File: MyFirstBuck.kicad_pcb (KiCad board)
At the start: 2 copper layers, 130.3 x 127 mm, 43 parts, among them J1 Conn_01x01_Pin, J2 Conn_01x01_Pin, J3 Conn_01x01_Pin, J4 Conn_01x01_Pin, J5 Conn_01x01_Pin, Q1 IRF540N, U1 LM358, U2 LAUNCHXL-F28379D, U3 UCC5304DWVR, U4 TMV 0512SHI

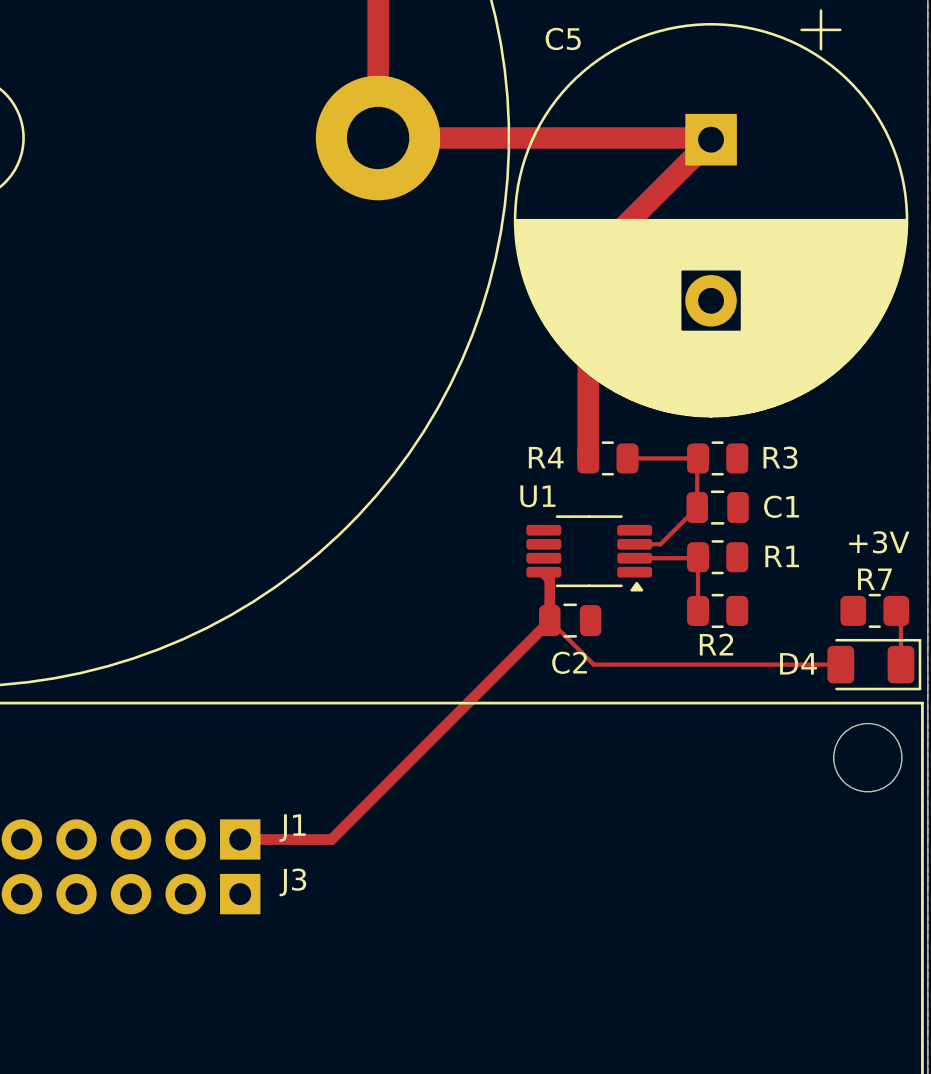
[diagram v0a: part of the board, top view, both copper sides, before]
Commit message: update on capacitor 1 to 560pF
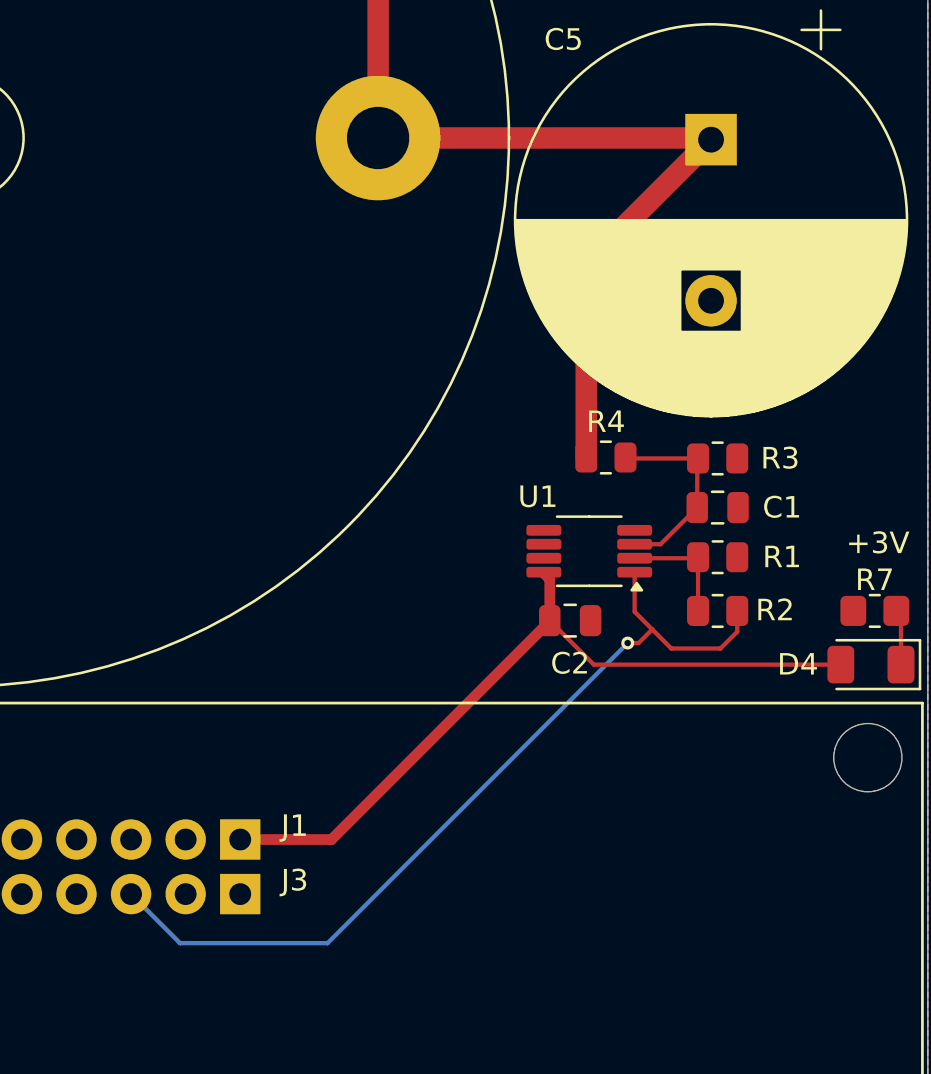
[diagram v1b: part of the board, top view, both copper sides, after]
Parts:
- C1: value ? -> 560pF
- R4: value ? -> 10k
- moved R4 0.10 mm to (188.2, 82.3), turned to 0 degrees
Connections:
- R4 pad 1: Net-(U1A-+) -> /VOUT
- R4 pad 2: /VOUT -> Net-(U1A-+)
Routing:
- net /VFILT: track 0.00 -> 39.9 mm, vias 0 -> 1

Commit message: New component changes
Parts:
- C1: value 560pF -> 6.8uF
- C2: value C -> 100NF
- R2, R3: value ? -> 600
- moved R3 0.13 mm to (193.3, 82.3), turned to 180 degrees
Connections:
- R3 pad 1: Net-(U1A-+) -> GND
- R3 pad 2: GND -> Net-(U1A-+)

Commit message: new updates
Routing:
- net /VG: track 14.2 -> 19.6 mm
- net /GD/PWM_FILT: track 8.16 -> 10.4 mm
- net Net-(D7-K): track 0.00 -> 2.10 mm
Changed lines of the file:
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@@
 		(tags "resistor")
 		(property "Reference" "R3"
-			(at -3.048 0 360)
+			(at -3.048 0 0)
 			(layer "F.SilkS")
 			(effects
@@
 		)
 		(property "Value" "600"
-			(at 0 1.65 360)
+			(at 0 1.65 0)
 			(layer "F.Fab")
 			(effects
@@
 		)
 		(fp_text user "${REFERENCE}"
-			(at 0 0 360)
+			(at 0 0 0)
 			(layer "F.Fab")
 			(effects
@@
 	)
 	(segment
+		(start 83.1012 69.458)
+		(end 84.6642 71.021)
+		(width 0.2)
+		(layer "F.Cu")
+		(net 23)
+	)
+	(segment
+		(start 78.4115 71.926)
+		(end 78.449 71.8885)
+		(width 0.2)
+		(layer "F.Cu")
+		(net 23)
+	)
+	(segment
+		(start 80.8795 69.458)
+		(end 83.1012 69.458)
+		(width 0.2)
+		(layer "F.Cu")
+		(net 23)
+	)
+	(segment
+		(start 75.949 71.926)
+		(end 78.4115 71.926)
+		(width 0.2)
+		(layer "F.Cu")
+		(net 23)
+	)
+	(segment
 		(start 78.449 71.8885)
 		(end 80.8795 69.458)
-		(width 0.2)
-		(layer "F.Cu")
-		(net 23)
-	)
-	(segment
-		(start 83.1012 69.458)
-		(end 84.6642 71.021)
-		(width 0.2)
-		(layer "F.Cu")
-		(net 23)
-	)
-	(segment
-		(start 78.4115 71.926)
-		(end 78.449 71.8885)
-		(width 0.2)
-		(layer "F.Cu")
-		(net 23)
-	)
-	(segment
-		(start 75.949 71.926)
-		(end 78.4115 71.926)
 		(width 0.2)
 		(layer "F.Cu")
@@
 	)
 	(segment
+		(start 108.227 66.017)
+		(end 108.227 63.818)
+		(width 0.2)
+		(layer "F.Cu")
+		(net 82)
+	)
+	(segment
+		(start 106.808 67.436)
+		(end 108.227 66.017)
+		(width 0.2)
+		(layer "F.Cu")
+		(net 82)
+	)
+	(segment
 		(start 105.479 70.676)
 		(end 105.479 67.506)
@@
 	(segment
 		(start 105.549 67.436)
+		(end 106.808 67.436)
+		(width 0.2)
+		(layer "F.Cu")
+		(net 82)
+	)
+	(segment
+		(start 105.549 67.436)
 		(end 113.597 67.436)
 		(width 1)
@@
 	)
 	(segment
+		(start 103.327 63.818)
+		(end 105.427 63.818)
+		(width 0.2)
+		(layer "F.Cu")
+		(net 89)
+	)
+	(segment

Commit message: updates
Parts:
- added L2: 10mH, 1140-103K-RC:INDRD2921W163D3810H2616P, F.Cu at (169.9, 73.9)
- C1: value 6.8uF -> 4.7uF
- C5: value ? -> 4.7uF; footprint Capacitor_THT:CP_Radial_D18.0mm_P7.50mm -> Capacitor_SMD:C_1206_3216Metric_Pad1.33x1.80mm_HandSolder
- L1: value ? -> 10mH; footprint Inductor_THT:L_Radial_D50.8mm_P38.86mm_Vishay_IHB-6 -> 1140-103K-RC:INDRD2921W163D3810H2616P
- moved L1 21.8 mm to (141.2, 45.7)
- moved U1 8.33 mm to (192.8, 80.3)
- moved C2 8.33 mm to (191.9, 83.5)
- moved R3 8.33 mm to (198.7, 75.9)
- moved R4 8.33 mm to (193.6, 75.9)
- moved C1 8.33 mm to (198.8, 78.2)
- moved R1 8.33 mm to (198.8, 80.6)
- moved R2 8.33 mm to (198.8, 83.1)
- moved C5 4.04 mm to (196.8, 69.2), turned to 0 degrees
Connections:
- L1 pad 2: /VOUT -> Net-(L1-Pad2)
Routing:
- net Net-(L1-Pad2): track 0.00 -> 28.4 mm
- net GND: track 0.00 -> 27.3 mm
- net /VOUT: track 73.8 -> 57.4 mm
- net /VFILT: track 39.9 -> 48.5 mm
- net /VSW: track 135.9 -> 144.3 mm
- net +3.3V: track 35.4 -> 41.4 mm

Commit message: new CSV uploaded
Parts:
- C7: value C -> 1u
- C9: value C -> 32pC
- R9: value R -> 51R
- moved C7 0.16 mm to (92.2, 78.2)
- renumbered D3 to D3(Red)1, D4 to D4(green)1, D5 to D5(Blue)1
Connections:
- L1 pad 1: /VSW -> (no net)
- L1 pad 2: Net-(L1-Pad2) -> (no net)
- L2 pad 1: Net-(L1-Pad2) -> (no net)
- L2 pad 2: /VOUT -> (no net)
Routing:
- net Net-(L1-Pad2): track 28.4 -> 0.00 mm
- net (no net): track 0.00 -> 28.4 mm

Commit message: Gerber and drill added
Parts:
- removed U1: LM358, Package_SO:VSSOP-8_3x3mm_P0.65mm
- added REF**: 61202021621, 61202021621:61202021621, F.Cu at (162.4, 144.5)
- added REF**: MountingHole_2.2mm_M2, MountingHole:MountingHole_2.2mm_M2, F.Cu at (205.2, 24.0)
- added REF**: MountingHole_2.2mm_M2, MountingHole:MountingHole_2.2mm_M2, F.Cu at (70.8, 24.0)
- added REF**: 61202021621, 61202021621:61202021621, F.Cu at (96.3, 144.5)
- added REF**: MountingHole_2.2mm_M2, MountingHole:MountingHole_2.2mm_M2, F.Cu at (70.8, 154.0)
- added REF**: MountingHole_2.2mm_M2, MountingHole:MountingHole_2.2mm_M2, F.Cu at (205.2, 154.0)
- added U5: LM358AP, LM358AP:P8, F.Cu at (165.7, 35.4)
- moved R1 48.7 mm to (178.1, 36.5)
- moved R2 48.7 mm to (178.1, 39.0)
- moved C1 48.7 mm to (178.1, 34.2)
- moved R4 48.7 mm to (172.9, 31.9)
- moved R3 48.6 mm to (178.1, 31.9)
- moved C2 43.1 mm to (166.8, 48.5)
- moved C5 20.5 mm to (195.5, 48.8), turned to 180 degrees
- moved J2 13.1 mm to (184.2, 48.2)
- moved L2 0.18 mm to (170.0, 73.8)
- moved L1 0.08 mm to (141.1, 45.8)
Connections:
- L1 pad 1: (no net) -> /VSW
- L1 pad 2: (no net) -> Net-(L1-Pad2)
- L2 pad 1: (no net) -> Net-(L1-Pad2)
- L2 pad 2: (no net) -> /VOUT
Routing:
- net GND: track 27.3 -> 252.5 mm, vias 4 -> 2
- net +3.3V: track 41.4 -> 90.6 mm
- net /VFILT: track 48.5 -> 85.4 mm
- net Net-(L1-Pad2): track 0.00 -> 28.4 mm
- net (no net): track 28.4 -> 0.00 mm
- net /VOUT: track 57.4 -> 76.3 mm
- net Net-(U5-1IN+): track 9.06 -> 11.5 mm
- net Net-(U5-1IN-): track 5.47 -> 7.06 mm
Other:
- board size 130.3 x 127 mm -> 139.5 x 135.1 mm
